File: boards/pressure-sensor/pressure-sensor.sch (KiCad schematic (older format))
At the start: 2 parts, among them J1 CONN_01X04_MALE

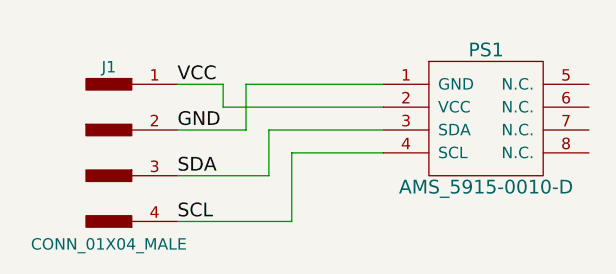
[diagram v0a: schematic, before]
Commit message: boards/pressure_sensor: all complains addressed
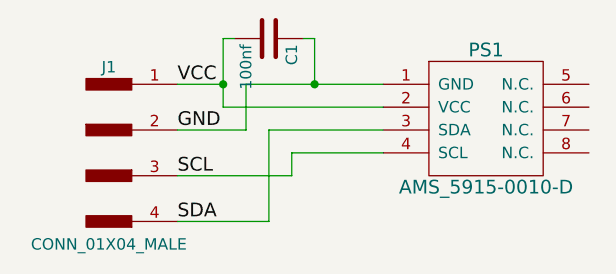
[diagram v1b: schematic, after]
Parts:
- added C1: 100nf, Capacitors_SMD:C_0603_HandSoldering, symbol C
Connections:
- net GND: now also C1.1
- net SCL: now also J1.3; no longer J1.4
- net SDA: now also J1.4; no longer J1.3
- net VCC: now also C1.2
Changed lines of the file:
@@
 LIBS:valves
 LIBS:rchojetzki-pressure-sensor-board
+LIBS:pressure-sensor-cache
 EELAYER 25 0
 EELAYER END
@@
 	1    0    0    -1
 $EndComp
-Wire Wire Line
-	1150 1300 1550 1300
-Wire Wire Line
-	1150 1500 1650 1500
 Text Label 1150 1100 0    60   ~ 0
 GND
 Text Label 1150 900  0    60   ~ 0
 VCC
+Text Label 1150 1500 0    60   ~ 0
+SDA
 Text Label 1150 1300 0    60   ~ 0
-SDA
-Text Label 1150 1500 0    60   ~ 0
 SCL
 Wire Wire Line
@@
 	1450 1100 1150 1100
 Wire Wire Line
-	2050 1000 1350 1000
+	1350 1000 2050 1000
 Wire Wire Line
-	1350 1000 1350 900
+	1350 700  1350 1000
 Wire Wire Line
 	1350 900  1150 900
 Wire Wire Line
-	1550 1300 1550 1100
+	1550 1100 1550 1500
 Wire Wire Line
 	1550 1100 2050 1100
 Wire Wire Line
 	2050 1200 1650 1200
+$Comp
+L C C1
+U 1 1 5910E751
+P 1550 700
+F 0 "C1" H 1575 800 50  0000 L CNN
+F 1 "100nf" H 1575 600 50  0000 L CNN
+F 2 "Capacitors_SMD:C_0603_HandSoldering" H 1588 550 50  0001 C CNN
+F 3 "" H 1550 700 50  0001 C CNN
+	1    1550 700
+	0    1    1    0
+$EndComp
 Wire Wire Line
-	1650 1200 1650 1500
+	1350 700  1400 700
+Connection ~ 1350 900
+Wire Wire Line
+	1700 700  1750 700
+Wire Wire Line
+	1750 700  1750 900
+Connection ~ 1750 900
+Wire Wire Line
+	1650 1300 1150 1300
+Wire Wire Line
+	1650 1200 1650 1300
+Wire Wire Line
+	1550 1500 1150 1500
 $EndSCHEMATC
